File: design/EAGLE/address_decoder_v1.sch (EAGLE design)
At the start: 10 parts, among them IC1 74LS08N, IC2 74LS04N, IC3 74LS00N, IC4 74LS21N, IC5 74LS32N, IC6 74LS32N, IC7 74LS02N, IC8 74LS02N

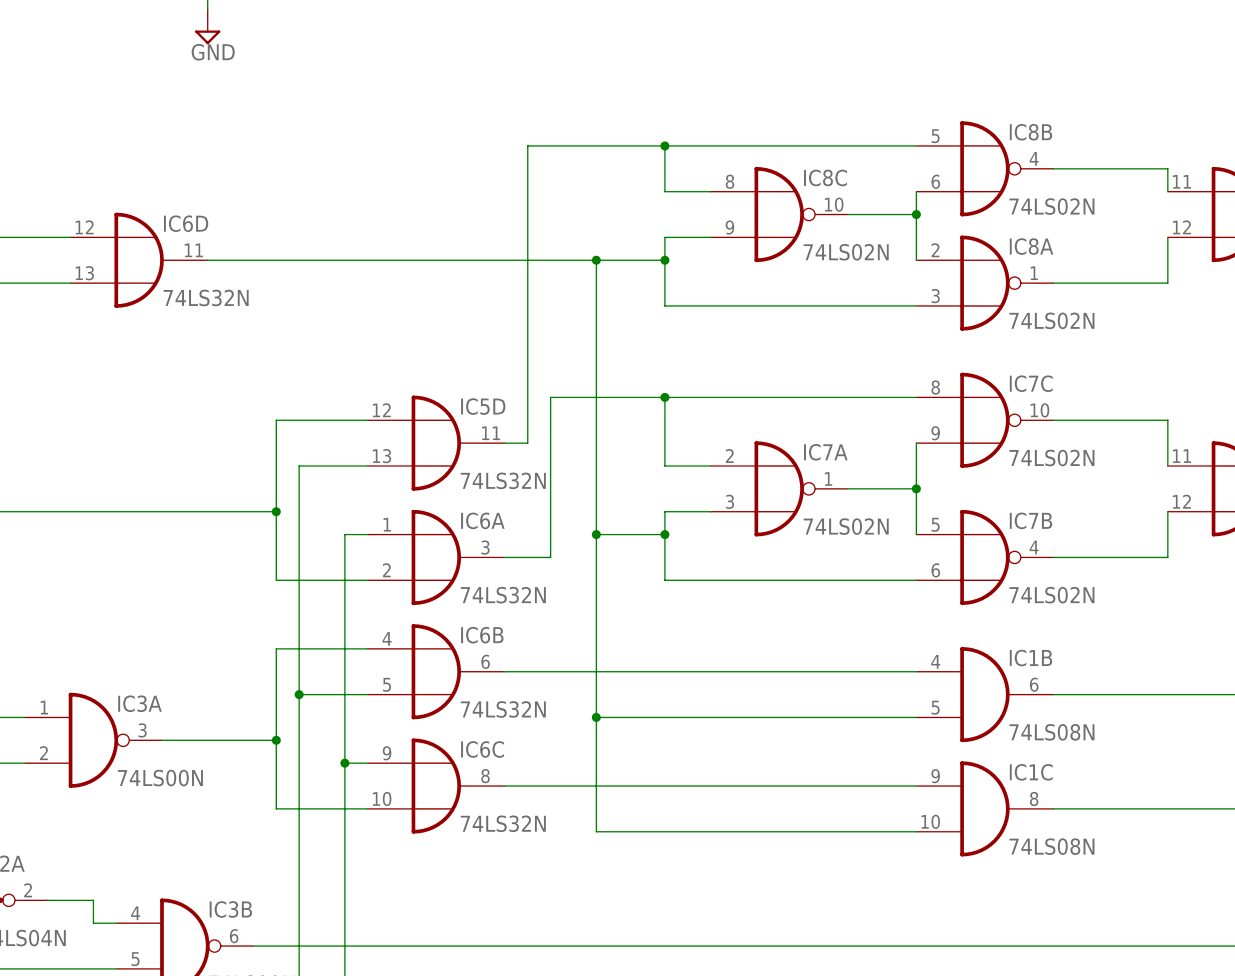
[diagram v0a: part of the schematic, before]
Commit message: Gate tidy up in prep for layout
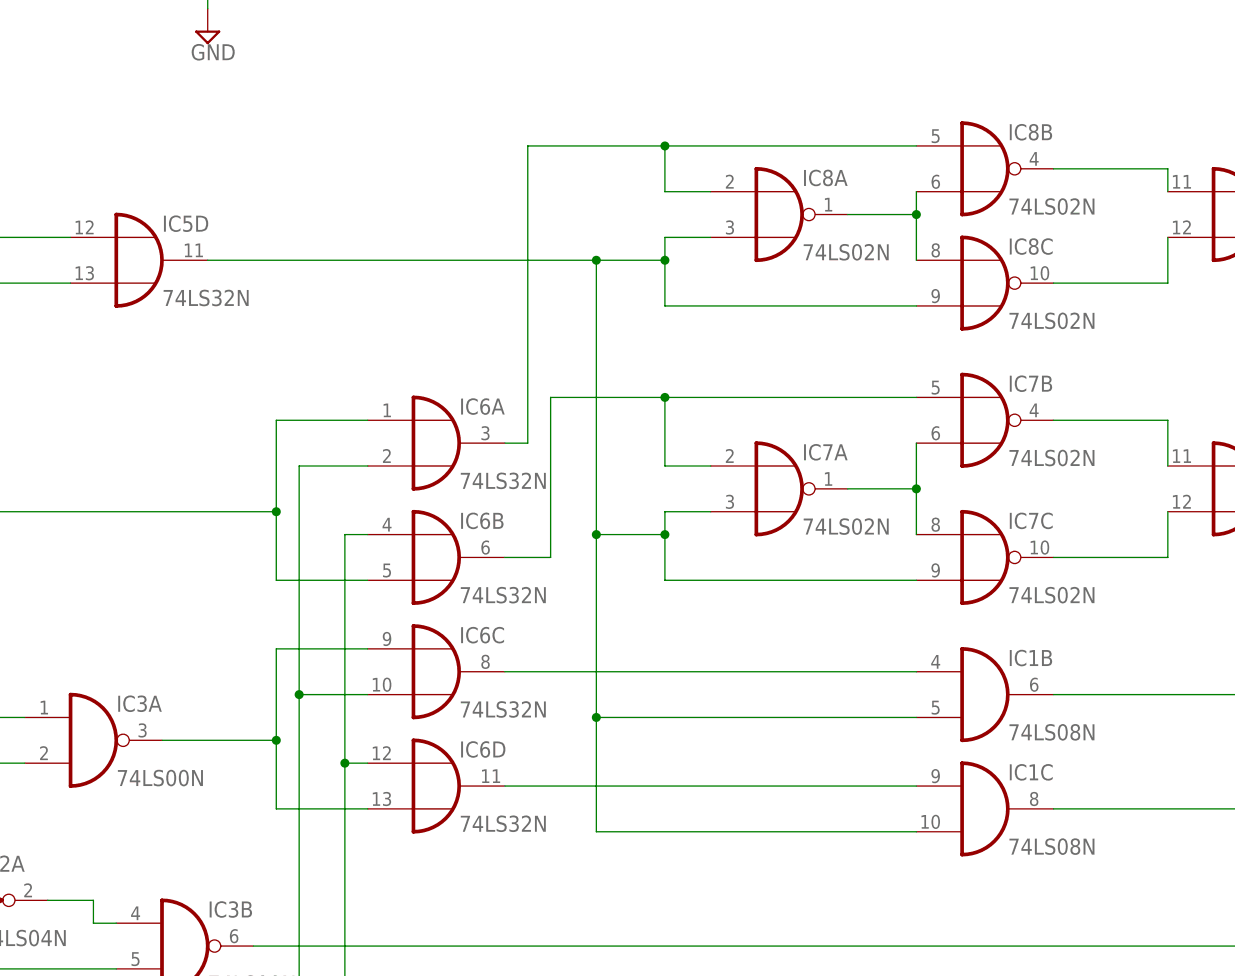
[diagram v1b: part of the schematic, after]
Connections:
- net /BOOT: now also IC5D.I0; no longer IC6D.I0
- net /LDS: now also IC6B.I0, IC6D.I0; no longer IC6A.I0, IC6C.I0
- net /UDS: now also IC6A.I1, IC6C.I1; no longer IC5D.I1, IC6B.I1
- net N$1: now also IC8A.O, IC8C.I0; no longer IC8A.I0, IC8C.O
- net N$10: now also IC7C.O; no longer IC7B.O
- net N$11: now also IC6C.O; no longer IC6B.O
- net N$12: now also IC6D.O; no longer IC6C.O
- net N$17: now also IC6C.I0, IC6D.I1; no longer IC6B.I0, IC6C.I1
- net N$20: now also IC5D.I1, IC6A.I0, IC6B.I1; no longer IC5D.I0, IC6A.I1, IC6D.I1
- net N$3: now also IC8C.O; no longer IC8A.O
- net N$4: now also IC6A.O, IC8A.I0; no longer IC5D.O, IC8C.I0
- net N$6: now also IC7B.I1, IC7C.I0; no longer IC7B.I0, IC7C.I1
- net N$7: now also IC7B.O; no longer IC7C.O
- net N$8: now also IC6B.O, IC7B.I0; no longer IC6A.O, IC7C.I0
- net N$9: now also IC5D.O, IC7C.I1; no longer IC6D.O, IC7B.I1
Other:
- moved on the sheet: IC5D, IC6A, IC6B, IC6C, IC6D, IC7B, IC7C, IC8A, IC8C
